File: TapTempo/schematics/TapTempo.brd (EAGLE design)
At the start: 60.6 x 50.3 mm, 48 parts, among them IC1 MEGA168, IC2 MCP4921, IC3 TL072D, IC4 LM4041A12DBZ, Q301 BC846, Q701 BC846, Y1 16Mhz

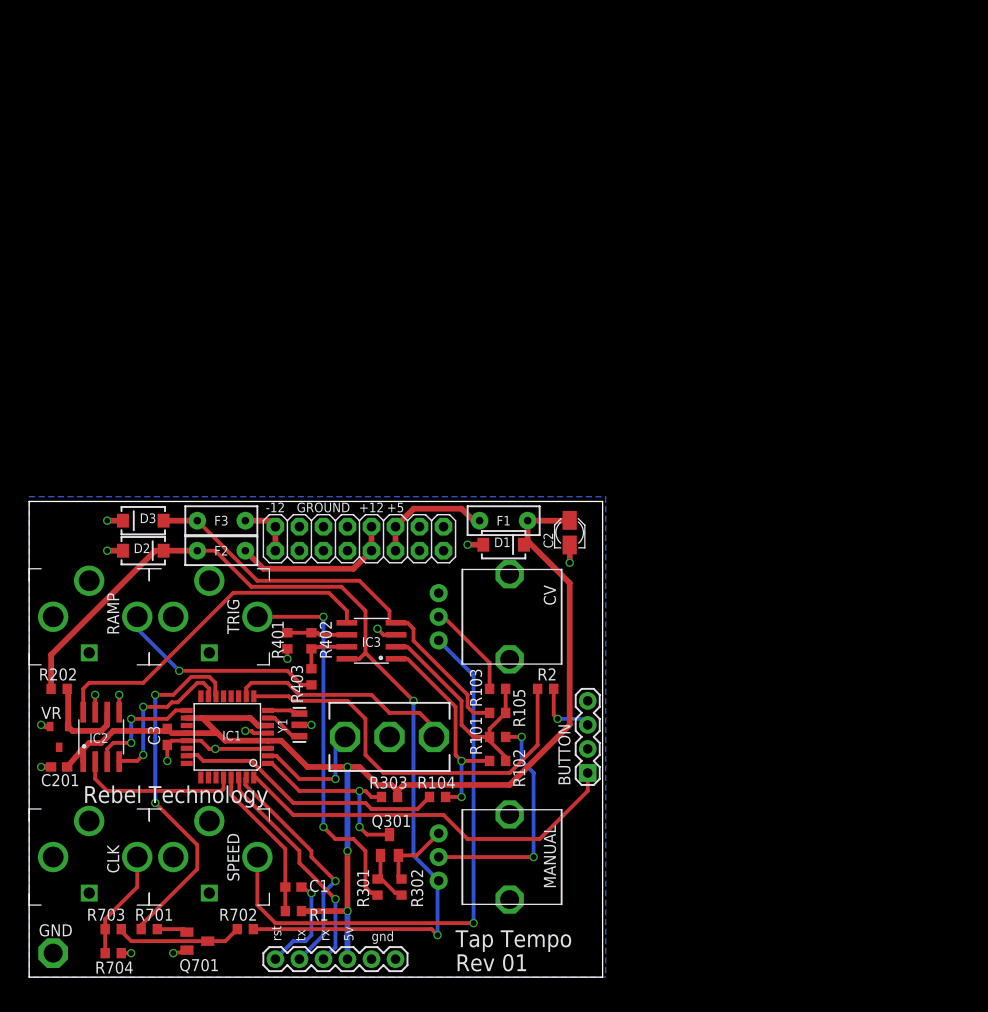
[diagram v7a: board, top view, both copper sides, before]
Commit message: stripped-down version based on Marsenne Twister design
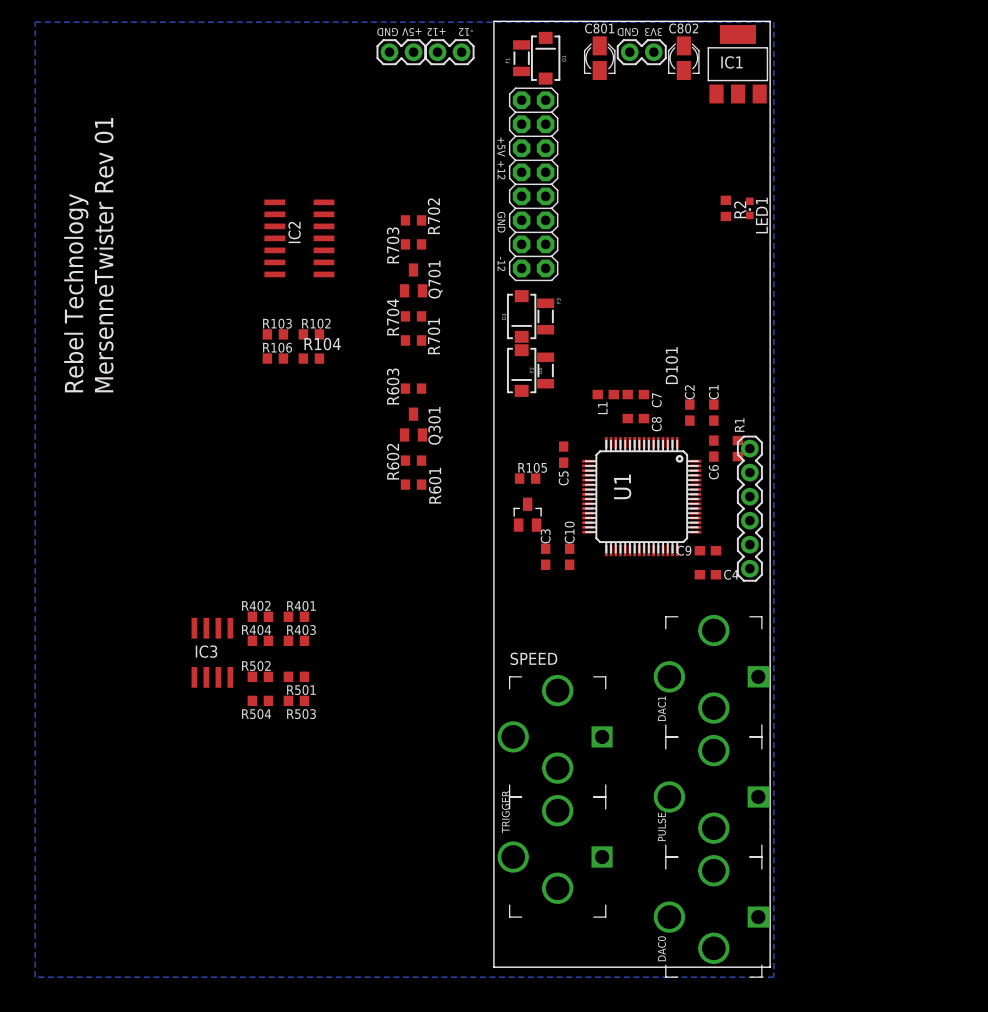
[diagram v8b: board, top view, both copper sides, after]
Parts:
- removed BUTTON: (no value), SparkFun:1X04
- removed C201: 100n, resistor:C0603
- removed CLK, RAMP, TRIG: PJ-301B, TomW:PJ-301B
- removed CV, MANUAL: POT-ALPS-RK09L1140, Rebel:POT-ALPS-RK09L1140
- removed GND: TPPAD1-20, testpad:P1-20
- removed IC4: LM4041A12DBZ, texas:DBZ_R-PDSO-G3
- removed R101: 120K, resistor:R0603
- removed R202: 1K, resistor:R0603
- removed R301: 100K, resistor:R0603
- removed R302: 1M, resistor:R0603
- removed R303: 10K, resistor:R0603
- removed S1: (no value), Rebel:SWITCH-SPDT-SALECOM-T8014
- removed U$1: (no value), Rebel:RT-LOGO-REBEL-BL
- removed Y1: 16Mhz, SparkFun:RESONATOR-SMD
- added C10, C5, C6, C8, C9: 100n, resistor:C0603
- added C4: 2u2, resistor:C0603
- added C7: 1u, resistor:C0603
- added C801, C802: 10u, resistor:PANASONIC_A
- added D101: BAT54S, diode:SOT23
- added DAC0, DAC1, PULSE, TRIGGER: JACK-PJ-301B, Rebel:PJ-301B
- added JP21, JP22, JP23: (no value), SparkFun:1X02
- added L1: INDUCTOR, Rebel:0603
- added LED1: (no value), led:CHIPLED_0603
- added R106: 120K, resistor:R0603
- added R404, R504: 100R, resistor:R0603
- added R501: 470k, resistor:R0603
- added R502: 100k, resistor:R0603
- added R503: 68k, resistor:R0603
- added R601: 100K, resistor:R0603
- added R602: 1M, resistor:R0603
- added R603: 10K, resistor:R0603
- added U1: STM32F10XRXT6, stm32:TQFP64
- C1: value 100n -> 1u
- C2: value 10u -> 100n; device resistor:PANASONIC_A -> resistor:C0603
- C3: value 100n -> 2u2
- F1, F2, F3: value PTCPTH -> PTCSMD; device Rebel:PTC -> SparkFun:PTC-1206
- IC1: value MEGA168 -> REG1117; device atmel:TQFP32-08 -> burr-brown:SOT223
- IC2: value MCP4921 -> TL074D; device Rebel:SOIC8 -> linear:SO14
- R104: value 51K -> 1K
- R105: value 120K -> 1K
- R2: value 10K -> 1K
- R401: value 120k -> 270k
- R402: value 120k -> 100k
- R403: value 100R -> 68k
- SPEED: value PJ-301B -> JACK-PJ-301B; device TomW:PJ-301B -> Rebel:PJ-301B
- U$3: device Rebel:RT-LOGO-TECH-BL -> Rebel:RT-LOGO-35MM-BL
- moved IC1 89.3 mm to (74.9, 96.5), turned to 0 degrees
- moved R703 79.0 mm to (40.6, 77.5), turned to 0 degrees
- moved R702 77.0 mm to (40.6, 80.0)
- moved R704 74.4 mm to (40.6, 69.8), turned to 0 degrees
- moved Q701 73.5 mm to (40.6, 73.7), turned to 0 degrees
- moved R701 68.2 mm to (40.6, 67.3), turned to 180 degrees
- moved R1 67.8 mm to (74.9, 55.9), turned to 90 degrees
- moved C1 67.0 mm to (72.4, 59.7), turned to 90 degrees
- moved JP1 65.7 mm to (76.2, 55.9), turned to 270 degrees
- moved IC2 56.7 mm to (28.6, 78.1), turned to 90 degrees
- moved R2 54.3 mm to (73.7, 81.3), turned to 270 degrees
- moved U$3 52.4 mm to (8.57, 65.1), turned to 90 degrees
- moved D1 51.6 mm to (54.6, 97.2), turned to 90 degrees
- moved R102 49.2 mm to (29.8, 67.9), turned to 0 degrees
- moved F1 48.9 mm to (52.1, 97.2), turned to 90 degrees
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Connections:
- removed net ALTA: IC1.9, R2.2
- removed net CS: IC1.28, IC2.2
- removed net DELIN: IC1.24
- removed net GATEIN: IC1.1, Q301.3, R303.2
- removed net LED+: BUTTON.3, R2.1
- removed net MODESW: IC1.10, S1.1
- removed net N$1: CV.3, SPEED.P$3
- removed net N$14: IC1.25
- removed net N$15: IC1.26
- removed net N$16: IC1.27
- removed net N$21: IC1.8, Y1.3
- removed net N$28: R301.1, TRIG.P$3
- removed net N$3: MANUAL.2, R101.1
- removed net N$39: C1.2, IC1.29, R1.1
- removed net N$9: IC3.6, R401.1, R402.1
- removed net RAMP: IC2.8, IC3.5
- removed net RX: IC1.30, JP1.4
- removed net SCK: IC1.17, IC2.3
- removed net SDI: IC1.15, IC2.4
- removed net SPEEDIN: IC1.23, R104.2
- removed net STOPSW: IC1.2, S1.3
- removed net TRIGIN: BUTTON.1, IC1.32
- removed net TRIGOUT: IC1.14, R701.1
- removed net TX: IC1.31, JP1.5
- removed net VREF: IC2.6, IC4.1, R202.2
- new net +3V3: C1.1, C10.1, C2.1, C5.1, C6.1, C802.+, C9.1, D101.2, IC1.2, JP1.1, JP21.1, L1.2, LED1.A, R603.1, U1.1, U1.19, U1.32, U1.48, U1.64
- new net ADC1: U1.11
- new net ADC2: U1.10
- new net ADC3: U1.9
- new net ADC4: R105.2, U1.15
- new net ADC5: U1.16
- new net ADC6: U1.8
- new net BOOT0: R1.1, U1.60
- new net DI0: Q301.3, R603.2, U1.50
- new net DI1: U1.28
- new net DO0: R701.1, U1.57
- new net DO1: U1.27
- new net N$13: IC3.2, R401.1, R402.1, R403.1
- new net N$18: IC3.6, R501.1, R502.1, R503.1
- new net N$19: LED1.C, R2.2
- new net N$23: R601.1, TRIGGER.TIP
- new net N$31: DAC0.TIP, R404.2
- new net N$32: DAC1.TIP, R504.2
- new net N$40: R103.1, SPEED.TIP
- new net NRST: JP1.5, U1.7
- new net PA0: U1.14
- new net PA10: U1.43
- new net PA11: U1.44
- new net PA12: U1.45
- new net PA3: U1.17
- new net PA4: R403.2, U1.20
- new net PA5: R503.2, U1.21
- new net PA6: U1.22
- new net PA7: U1.23
- new net PA8: U1.41
- new net PA9: U1.42
- new net PB0: U1.26
- new net PB10: U1.29
- new net PB11: U1.30
- new net PB12: U1.33
- new net PB13: U1.34
- new net PB14: U1.35
- new net PB15: U1.36
- new net PB4: U1.56
- new net PB6: U1.58
- new net PB7: U1.59
- new net PB8: U1.61
- new net PB9: U1.62
- new net PC10: U1.51
- new net PC11: U1.52
- new net PC12: U1.53
- new net PC13: U1.2
- new net PC14: U1.3
- new net PC15: U1.4
- new net PC4: U1.24
- new net PC5: U1.25
- new net PC6: U1.37
- new net PC7: U1.38
- new net PC8: U1.39
- new net PC9: U1.40
- new net PD2: U1.54
- new net SWCLK: JP1.2, U1.49
- new net SWDIO: JP1.4, U1.46
- new net SWO: JP1.6, U1.55
- new net V+: IC2.4
- new net V-: IC2.11
- new net VCAP_1: C3.1, U1.31
- new net VCAP_2: C4.1, U1.47
- new net VDDA: C7.1, C8.1, L1.1, U1.13
- net +12V: now also F2.2, JP23.1; no longer F2.P$2, MANUAL.3, R202.1
- net +5V: now also C801.+, F1.2, IC1.3, JP22.1; no longer C2.+, C201.1, C3.1, F1.P$2, IC1.18, IC1.20, IC1.4, IC1.6, IC2.1, JP1.3, R1.2, R303.1
- net -12V: now also F3.2, JP23.2, R106.1, R401.2, R501.2; no longer F3.P$1, R105.1
- net GND: now also C1.2, C10.2, C2.2, C4.2, C5.2, C6.2, C7.2, C8.2, C801.-, C802.-, C9.2, D101.1, DAC0.SHL, DAC0.SLV, DAC1.SHL, DAC1.SLV, IC1.1, IC2.13, IC3.5, JP1.3, JP21.2, JP22.2, PULSE.SHL, PULSE.SLV, R1.2, R2.1, R602.2, SPEED.SHL, SPEED.SLV, SPEED.SW, TRIGGER.SHL, TRIGGER.SLV, TRIGGER.SW, U1.12, U1.18, U1.63; no longer BUTTON.2, BUTTON.4, C2.-, C201.2, CLK.P$1, CLK.P$2, CV.1, CV.P$5, CV.P$6, GND.TP, IC1.21, IC1.3, IC1.5, IC2.5, IC2.7, IC4.2, JP1.1, JP1.2, MANUAL.1, MANUAL.P$5, MANUAL.P$6, R302.2, R401.2, RAMP.P$1, RAMP.P$2, S1.2, SPEED.P$1, SPEED.P$2, SPEED.P$4, TRIG.P$1, TRIG.P$2, TRIG.P$4, Y1.2
- net N$2: now also IC2.12, R106.2; no longer IC3.2, R101.2, R105.2
- net N$20: now also D101.3, R104.2, R105.1; no longer IC1.7, Y1.1
- net N$27: now also R601.2, R602.1; no longer R301.2, R302.1
- net N$29: now also DAC1.SW; no longer C1.1, JP1.6
- net N$35: now also PULSE.TIP; no longer CLK.P$3
- net N$4: now also IC2.14; no longer IC3.1
- net N$44: now also F1.1; no longer F1.P$1
- net N$45: now also F2.1; no longer F2.P$1
- net N$5: now also IC3.7, R502.2, R504.1; no longer CV.2, R103.1
- net N$6: now also F3.1; no longer F3.P$2
- net N$7: now also IC3.1, R404.1; no longer IC3.7, R403.1
- net N$8: now also DAC0.SW; no longer R403.2, RAMP.P$3
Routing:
- net +5V: track 127.5 -> 0.00 mm, vias 3 -> 0
- net +12V: track 103.5 -> 0.00 mm, vias 2 -> 0
- net N$1: track 60.1 -> 0.00 mm, vias 1 -> 0
- net -12V: track 45.1 -> 0.00 mm
- net GND: track 43.2 -> 0.00 mm, vias 16 -> 0
- net ALTA: track 42.7 -> 0.00 mm
- net TRIGIN: track 42.0 -> 0.00 mm
- net N$28: track 40.1 -> 0.00 mm, vias 2 -> 0
- net TRIGOUT: track 37.9 -> 0.00 mm, vias 2 -> 0
- net RAMP: track 36.6 -> 0.00 mm
- net SPEEDIN: track 28.6 -> 0.00 mm
- net N$3: track 25.0 -> 0.00 mm, vias 2 -> 0
- net TX: track 24.8 -> 0.00 mm, vias 1 -> 0
- net N$2: track 24.3 -> 0.00 mm
- net RX: track 24.0 -> 0.00 mm, vias 1 -> 0
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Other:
- board size 60.6 x 50.3 mm -> 29.2 x 100 mm
- board text added: "+5V"
- board text added: "3V3"
- board text added: "GND"
- board text added: "MersenneTwister Rev 01"
- board text removed: "+5"
- board text removed: "-12v"
- board text removed: "5v"
- board text removed: "GROUND"
- board text removed: "Rev 01"
- board text removed: "Tap Tempo"
- board text removed: "VR"
- board text removed: "gnd"
- board text removed: "rst"
- board text removed: "rx"
- board text removed: "tx"
